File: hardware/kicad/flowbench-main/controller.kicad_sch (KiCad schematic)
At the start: 10 parts, among them U2 ESP32-S3-DevKitC-1-N32R8V

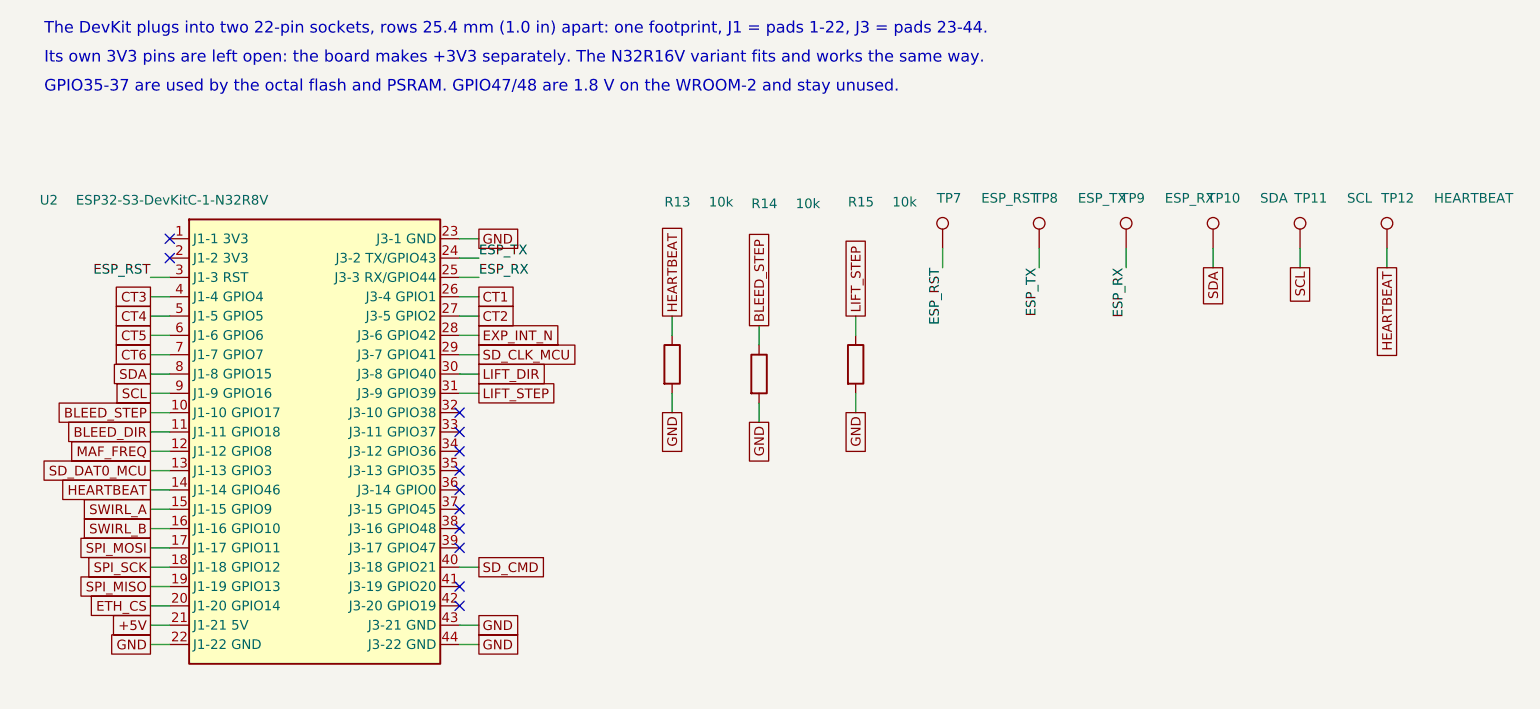
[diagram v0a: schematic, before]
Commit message: KiCad: 180 x 125 mm layout, status LEDs, grouped test-point areas
- Board shrinks from 220 x 160 to 180 x 125 mm with connectors on all four
  edges; 1.0 mm between parts kept for hand soldering.
- 24 status LEDs: power rails, eFuse fault, stepper alarms, watchdog, armed,
  stepper power, each contactor coil, and every switch input (in series with
  its opto, no extra resistor).
- Scattered test points replaced by grouped areas: 24 V loops, logic-supply
  loops, and controller, analog and Digimatic 2-row headers with a GND row.
  No test points on SPI/SD lines.
- LED, test point and test header labels stay on the silkscreen.

Co-Authored-By: Claude Opus 5.5 <noreply@anthropic.com>
Claude-Session: https://claude.ai/code/session_01QEmmugJA9S77dSDSNcKrPa
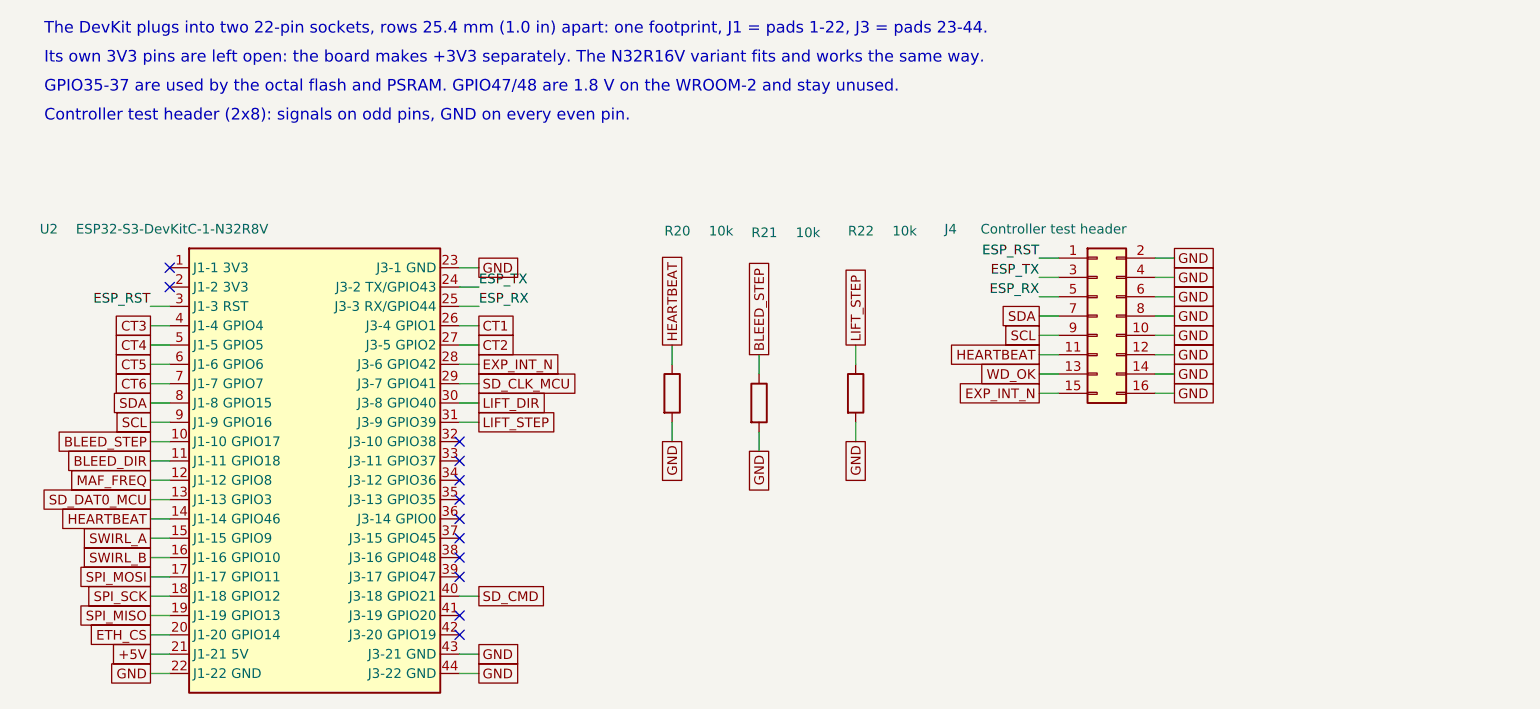
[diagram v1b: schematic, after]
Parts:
- removed R13, R14, R15: 10k, Resistor_SMD:R_0805_2012Metric, symbol FlowBench:R
- removed TP10: SDA, TestPoint:TestPoint_Loop_D2.50mm_Drill1.0mm, symbol FlowBench:TestPoint
- removed TP11: SCL, TestPoint:TestPoint_Loop_D2.50mm_Drill1.0mm, symbol FlowBench:TestPoint
- removed TP12: HEARTBEAT, TestPoint:TestPoint_Loop_D2.50mm_Drill1.0mm, symbol FlowBench:TestPoint
- removed TP7: ESP_RST, TestPoint:TestPoint_Loop_D2.50mm_Drill1.0mm, symbol FlowBench:TestPoint
- removed TP8: ESP_TX, TestPoint:TestPoint_Loop_D2.50mm_Drill1.0mm, symbol FlowBench:TestPoint
- removed TP9: ESP_RX, TestPoint:TestPoint_Loop_D2.50mm_Drill1.0mm, symbol FlowBench:TestPoint
- added J4: Controller test header, Connector_PinHeader_2.54mm:PinHeader_2x08_P2.54mm_Vertical, symbol FlowBench:Conn_02x08_Odd_Even
- added R20, R21, R22: 10k, Resistor_SMD:R_0805_2012Metric, symbol FlowBench:R
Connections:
- net BLEED_STEP: now also R21.1
- net ESP_RST: now also J4.1 (Pin_1)
- net ESP_RX: now also J4.5 (Pin_5)
- net ESP_TX: now also J4.3 (Pin_3)
- net EXP_INT_N: now also J4.15 (Pin_15)
- net GND: now also J4.10 (Pin_10), J4.12 (Pin_12), J4.14 (Pin_14), J4.16 (Pin_16), J4.2 (Pin_2), J4.4 (Pin_4), J4.6 (Pin_6), J4.8 (Pin_8), R20.2, R21.2, R22.2
- net HEARTBEAT: now also J4.11 (Pin_11), R20.1
- net LIFT_STEP: now also R22.1
- net SCL: now also J4.9 (Pin_9)
- net SDA: now also J4.7 (Pin_7)
- new net WD_OK: J4.13 (Pin_13)
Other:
- note added: "Controller test header (2x8): signals on odd pins, GND on every even pin."
- moved on the sheet: U2
